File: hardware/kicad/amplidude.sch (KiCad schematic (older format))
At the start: 0 parts

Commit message: Capture of app note for typical Single-Ended (SE) Configuration (8ohm speaker)
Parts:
- added C1, C2, C3, C4, C5, C6: 1u, symbol C
- added C10, C12: 10u, symbol C
- added C13, C14, C17, C18: 470u, symbol CP1
- added C15, C16: 220n, symbol C
- added C7, C9, C? (x2): 0.1u, symbol C
- added L1, L2: 33u, symbol L
- added R1, R2: R, symbol R
- added R3, R4: 4.7k, symbol R
- added U?: PAM8124, Housings_SSOP:TSSOP-24_4.4x7.8mm_Pitch0.65mm, symbol PAM8124
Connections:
- new net: C3.2, U?.11 (VCLAMP)
- new net: C6.1, L2.2, U?.15 (ROUT)
- new net: C6.2, U?.16 (BSR)
- new net: C5.2, U?.21 (BSL)
- new net: C5.1, L1.1, U?.22 (LOUT)
- new net: R1.1, U?.5 (LIN)
- new net: R2.1, U?.6 (RIN)
- new net: C4.1, U?.7 (VCM)
- new net: C1.1, R1.2
- new net: C2.1, R2.2
- new net: C15.2, C17.1, L1.2, R3.2
- new net: C16.2, C18.1, L2.1, R4.2
- new net +12V: C10.1, C12.1, C13.1, C14.1, C7.1, C9.1, C?.1, C?.1, U?.1 (PVCCL), U?.10 (PVCCR), U?.12 (PVCCR), U?.19 (SE_BTL), U?.20 (AVCC), U?.3 (PVCCL)
- new net AGND: C10.2, C12.2, C13.2, C14.2, C15.1, C16.1, C3.1, C4.2, C7.2, C9.2, C?.2, C?.2, R3.1, R4.1, U?.13 (PGNDR), U?.14 (PGNDR), U?.23 (PGNDL), U?.24 (PGNDL), U?.8 (AGND), U?.9 (AGND)
- new net G0: U?.18 (GAIN0)
- new net G1: U?.17 (GAIN1)
- new net L_IN: C1.2
- new net L_OUT+: C17.2
- new net MUTE: U?.4 (MUTE)
- new net R_IN: C2.2
- new net R_OUT+: C18.2
- new net SHUTDOWN: U?.2 (SDN)

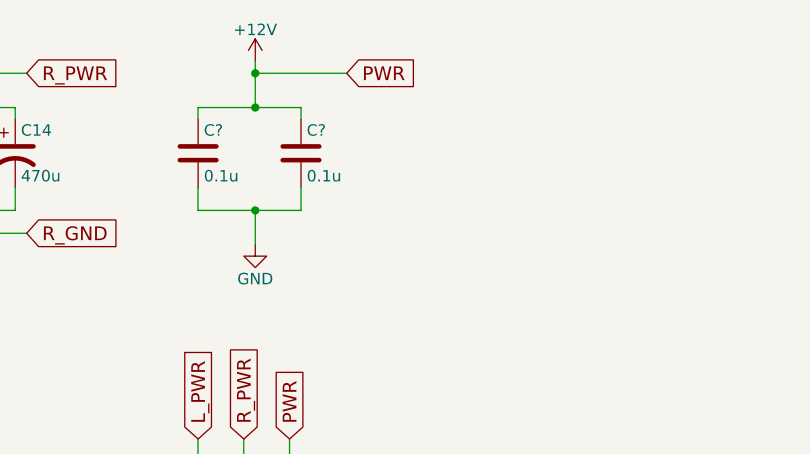
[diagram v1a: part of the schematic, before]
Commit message: Fix values of power capacitors
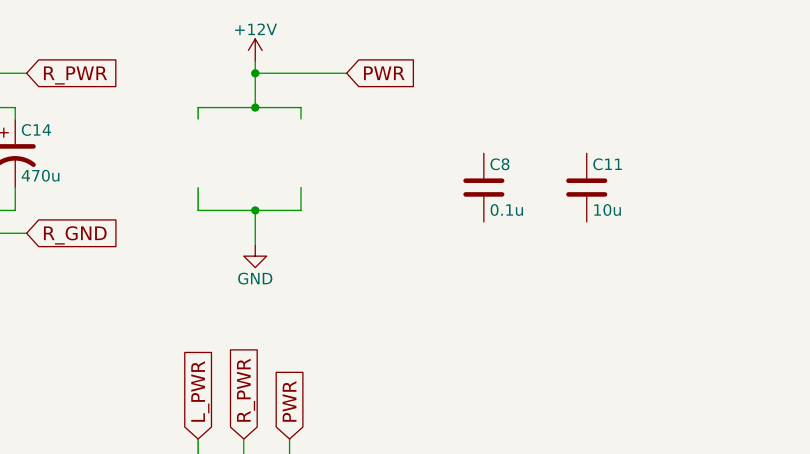
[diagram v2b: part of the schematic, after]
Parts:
- C11: renamed from C?; value 0.1u -> 10u
- gave numbers to parts that had none: 1
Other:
- moved on the sheet: C11, C8
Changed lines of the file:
@@
 $EndComp
 $Comp
-L C C?
+L C C8
 U 1 1 596B82C4
-P 5150 1850
-F 0 "C?" H 5175 1950 50  0000 L CNN
-F 1 "0.1u" H 5175 1750 50  0000 L CNN
-F 2 "" H 5188 1700 50  0001 C CNN
-F 3 "" H 5150 1850 50  0001 C CNN
-	1    5150 1850
+P 6400 2000
+F 0 "C8" H 6425 2100 50  0000 L CNN
+F 1 "0.1u" H 6425 1900 50  0000 L CNN
+F 2 "" H 6438 1850 50  0001 C CNN
+F 3 "" H 6400 2000 50  0001 C CNN
+	1    6400 2000
 	1    0    0    -1
 $EndComp
 $Comp
-L C C?
+L C C11
 U 1 1 596B838A
-P 5600 1850
-F 0 "C?" H 5625 1950 50  0000 L CNN
-F 1 "0.1u" H 5625 1750 50  0000 L CNN
-F 2 "" H 5638 1700 50  0001 C CNN
-F 3 "" H 5600 1850 50  0001 C CNN
-	1    5600 1850
+P 6850 2000
+F 0 "C11" H 6875 2100 50  0000 L CNN
+F 1 "10u" H 6875 1900 50  0000 L CNN
+F 2 "" H 6888 1850 50  0001 C CNN
+F 3 "" H 6850 2000 50  0001 C CNN
+	1    6850 2000
 	1    0    0    -1
 $EndComp
